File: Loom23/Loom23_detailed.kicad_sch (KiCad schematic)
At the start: 8 parts

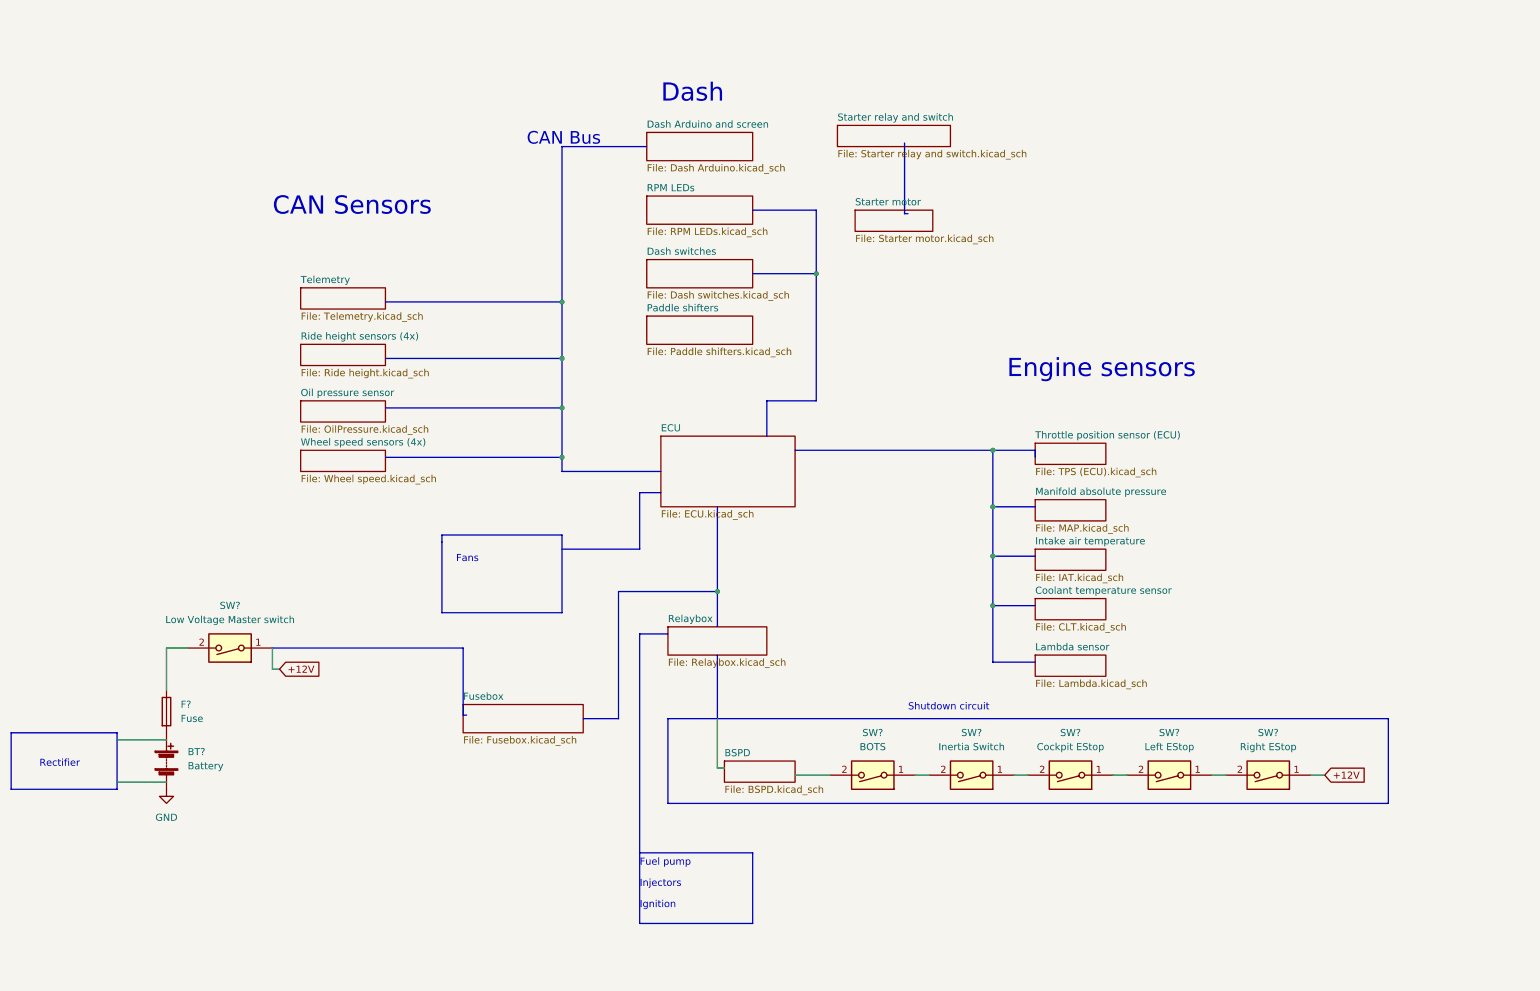
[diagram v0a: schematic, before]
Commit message: Added detailed version of schematic
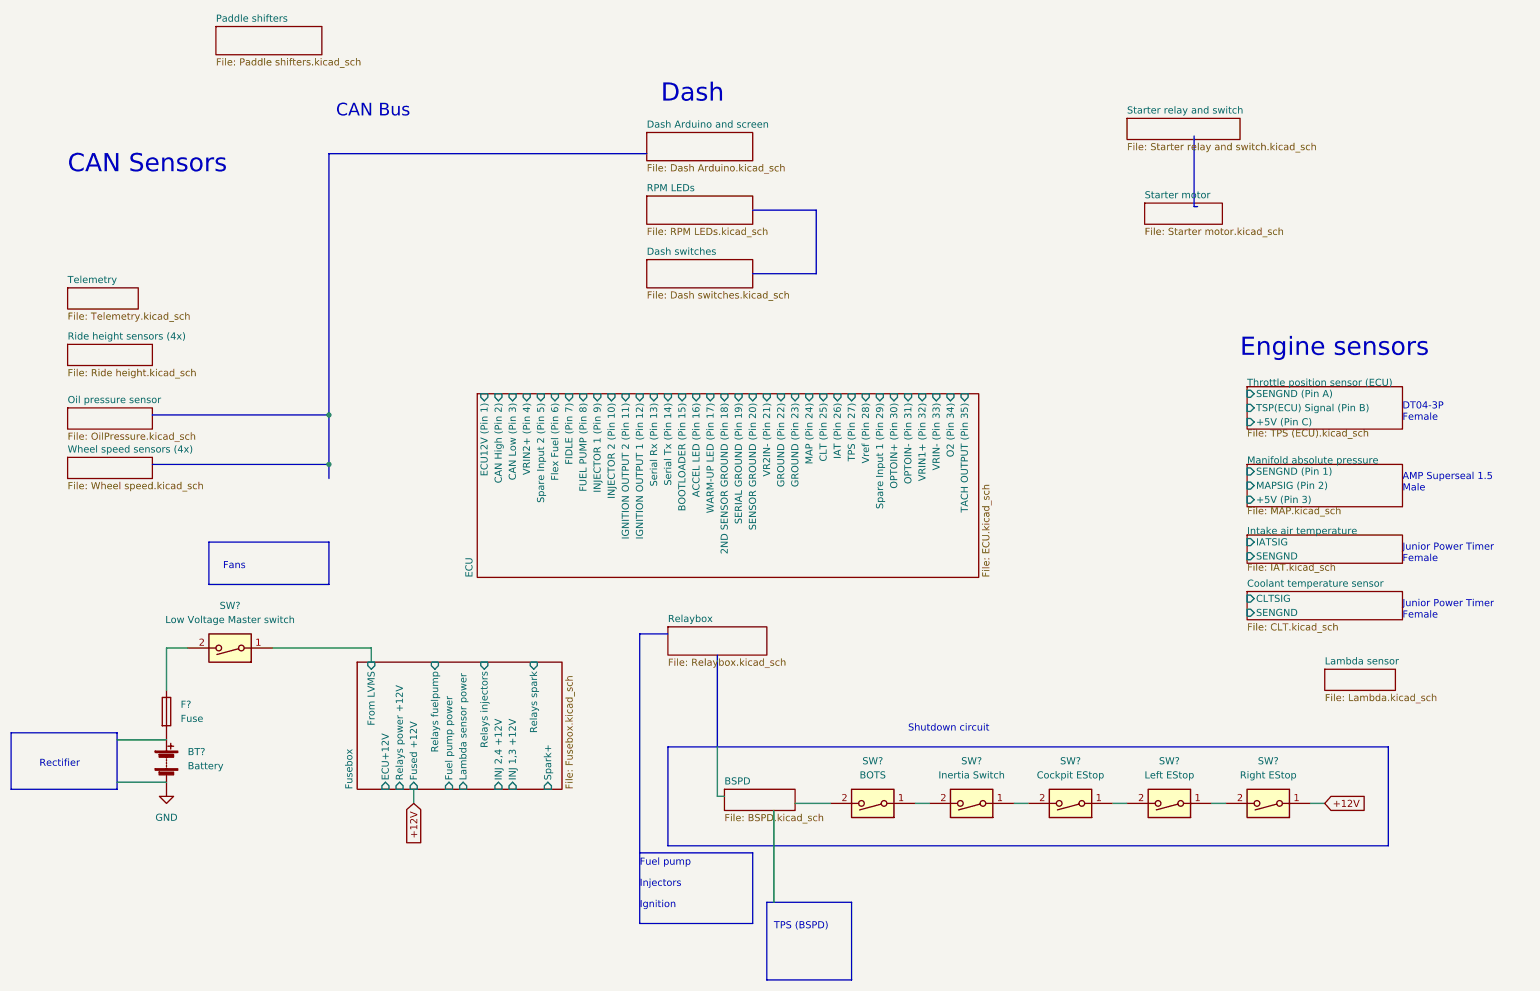
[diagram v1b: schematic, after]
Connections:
- net +12V: no longer SW?.1
- new net Fusebox/From LVMS: SW?.1
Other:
- sheet Coolant temperature sensor ports: added CLTSIG, SENGND; removed none
- sheet ECU ports: added 2ND SENSOR GROUND (Pin 18), ACCEL LED (Pin 16), BOOTLOADER (Pin 15), CAN High (Pin 2), CAN Low (Pin 3), CLT (Pin 25), ECU12V (Pin 1), FIDLE (Pin 7), FUEL PUMP (Pin 8), Flex Fuel (Pin 6), GROUND (Pin 22), GROUND (Pin 23), IAT (Pin 26), IGNITION OUTPUT 1 (Pin 12), IGNITION OUTPUT 2 (Pin 11), INJECTOR 1 (Pin 9), INJECTOR 2 (Pin 10), MAP (Pin 24), O2 (Pin 34), OPTOIN+ (Pin 30), OPTOIN- (Pin 31), SENSOR GROUND (Pin 20), SERIAL GROUND (Pin 19), Serial Rx (Pin 13), Serial Tx (Pin 14), Spare Input 1 (Pin 29), Spare Input 2 (Pin 5), TACH OUTPUT (Pin 35), TPS (Pin 27), VR2IN- (Pin 21), VRIN- (Pin 33), VRIN1+ (Pin 32), VRIN2+ (Pin 4), Vref (Pin 28), WARM-UP LED (Pin 17); removed none
- sheet Fusebox ports: added ECU+12V, From LVMS, Fuel pump power, Fused +12V, INJ 1,3 +12V, INJ 2,4 +12V, Lambda sensor power, Relays fuelpump, Relays injectors, Relays power +12V, Relays spark, Spark+; removed none
- sheet Intake air temperature ports: added IATSIG, SENGND; removed none
- sheet Manifold absolute pressure ports: added +5V (Pin 3), MAPSIG (Pin 2), SENGND (Pin 1); removed none
- sheet Throttle position sensor (ECU) ports: added +5V (Pin C), SENGND (Pin A), TSP(ECU) Signal (Pin B); removed none
- note added: "AMP Superseal 1.5 Male"
- note added: "DT04-3P Female"
- note added: "Junior Power Timer Female"
- note added: "TPS (BSPD)"
- moved on the sheet: SW?

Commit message: Signed-off-by: fst29 <fst29@cam.ac.uk>
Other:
- added sheet Ignition (ignition.kicad_sch)
- added sheet Injector1 (Injector.kicad_sch)
- added sheet Injector2 (Injector.kicad_sch)
- added sheet Injector3 (Injector.kicad_sch)
- added sheet Injector4 (Injector.kicad_sch)
- sheet Lambda sensor ports: added +12V, GND, O2SIG; removed none
- sheet Relaybox ports: added +12V, Fuel pump enable (ECU), Paddle shifter, Relayed Injectors, Relayed fuel pump, RelayedSpark, Shutdown signal; removed none
- note added: "Connector TBC"
- note added: "Pairing and connector type TBC"
- note removed: "Ignition"
- note removed: "Injectors"
- moved on the sheet: BT?, F?, SW?

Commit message: Added fuel pump, TPS(BSPD), BPS.
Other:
- added sheet BPS (BPS.kicad_sch)
- added sheet Fuel Pump (fuelPump.kicad_sch)
- added sheet TPS (BSPD) (TPS(BSPD).kicad_sch)
- sheet Lambda sensor ports: added +12V (Pin  C), GND (Pin A), O2SIG (Pin B); removed +12V, GND, O2SIG
- note added: "Pairing and connector type TBC High impedance injectors, no extra resistors needed."
- note removed: "Connector TBC"
- note removed: "Fuel pump"
- note removed: "Pairing and connector type TBC"
- note removed: "TPS (BSPD)"

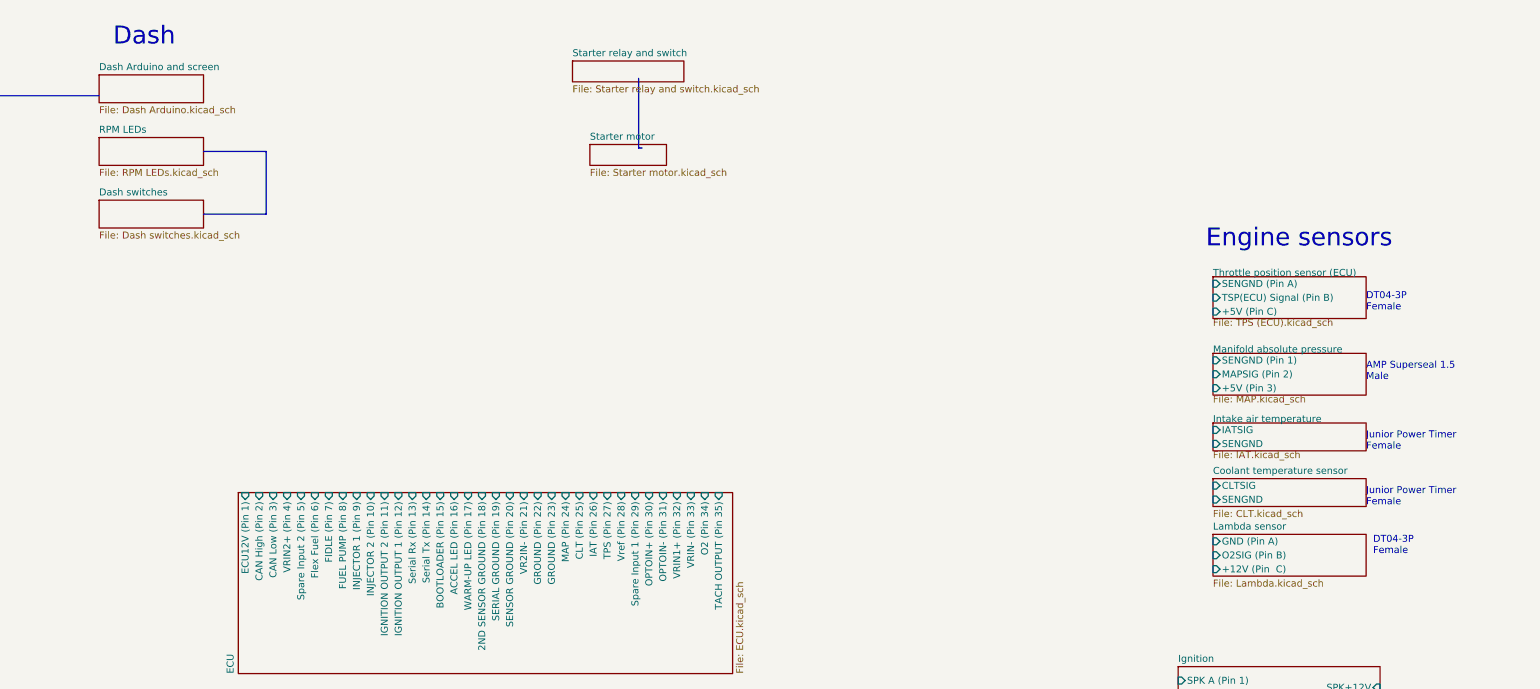
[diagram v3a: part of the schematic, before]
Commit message: Added dash switches and crank sensor.
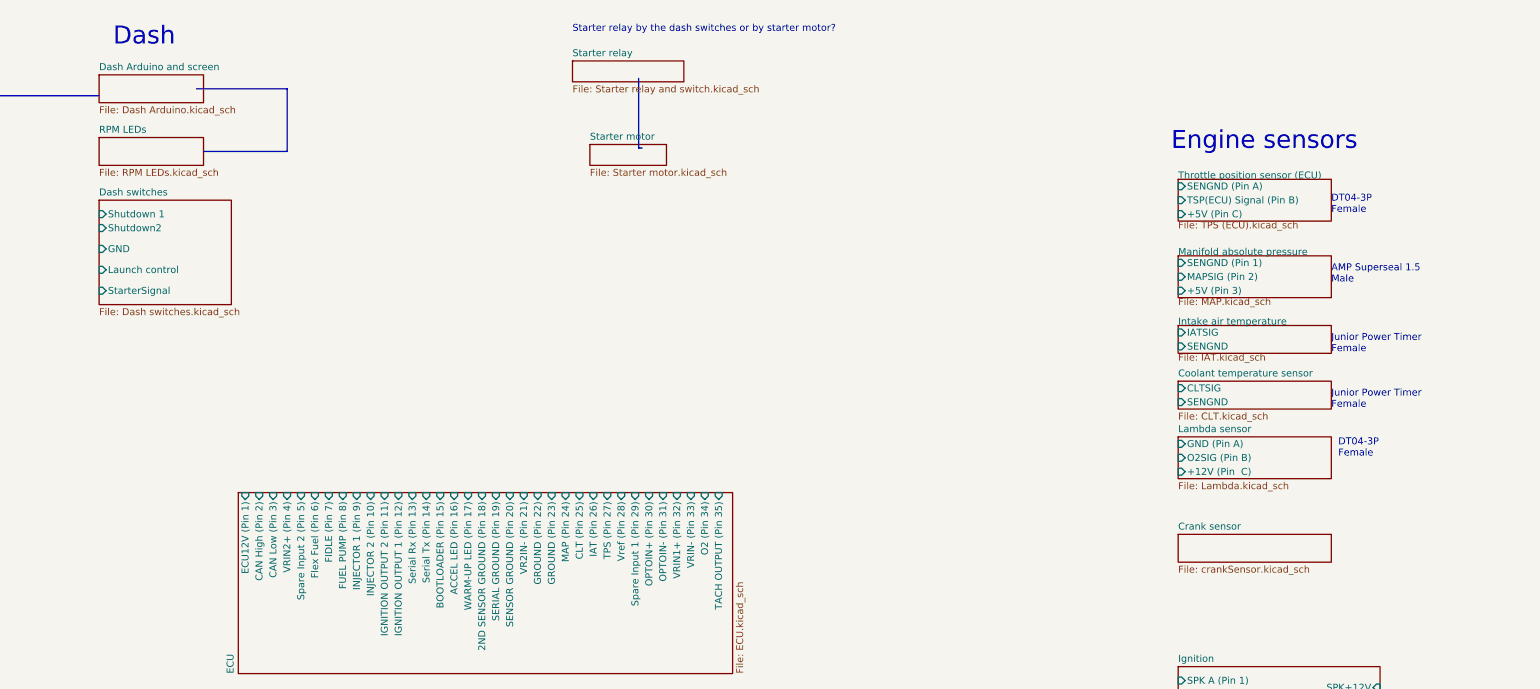
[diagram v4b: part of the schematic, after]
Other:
- sheet Starter relay and switch renamed Starter relay
- added sheet Crank sensor (crankSensor.kicad_sch)
- sheet Dash switches ports: added GND, Launch control, Shutdown 1, Shutdown2, StarterSignal; removed none
- note added: "Starter relay by the dash switches or by starter motor?"

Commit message: Added fans and their control circuit. Added some wires.
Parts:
- removed SW?: Cockpit EStop, symbol Switch:SW_DIP_x01
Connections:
- net +12V is gone; now on net Fusebox/From LVMS: SW?.1
- net Dash switches/Shutdown 1: now also SW?.2
- net Fusebox/From LVMS: now also SW?.2; no longer SW?.1
- net Relaybox/Shutdown signal: now also SW?.2
- net at F?.1: now also SW?.1; no longer SW?.2
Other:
- added sheet Cam sensor (CamSensor.kicad_sch)
- added sheet Cooling fan (left) (CoolingFan.kicad_sch)
- added sheet Cooling fan (rear) (CoolingFan.kicad_sch)
- added sheet Cooling fan (right) (CoolingFan.kicad_sch)
- sheet Dash switches ports: added Fan signal; removed none
- sheet Relaybox ports: added Fan signal, Relayed Fan; removed none
- note added: "Confirm pairing"
- note added: "FRONT OF CAR"
- note removed: "Fans"
- note removed: "Shutdown circuit"
- note removed: "Starter relay by the dash switches or by starter motor?"
- moved on the sheet: BT?, F?, SW?

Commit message: Finished wiring up the ECU.
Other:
- sheet Dash switches ports: added SerialGND, SerialRX, SerialTX; removed none
- note added: "Confirm spark order"
- note added: "Do NOT connect the LAMBDA GND to the Sensor ground of the ECU!"
- note added: "Good engine ground for ECU"
- note added: "Taped up and left floating"
- moved on the sheet: BT?, F?, SW?

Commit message: Added dash/wheel connections
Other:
- sheet RPM LEDs renamed RPM LEDs and wheel buttons
- removed sheet Wheel speed sensors (4x)
- added sheet Dash Break-out-board (DashBoB.kicad_sch)
- sheet Dash Arduino and screen ports: added +12V, CANH, CANL, GND, I2C (SCL), I2C (SDA); removed none
- sheet Paddle shifters ports: added +12V, GND, Paddle shift down, Paddle shift neutral, Paddle shift up, SparkStop; removed none
- sheet RPM LEDs and wheel buttons ports: added +12V, GND, I2C (SCL), I2C (SDA), Paddle shift down, Paddle shift neutral, Paddle shift up, TACH; removed none
- sheet Starter motor ports: added +12V, GND; removed none
- moved on the sheet: SW?
